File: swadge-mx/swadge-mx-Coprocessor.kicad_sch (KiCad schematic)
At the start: 6 parts, among them J4 Conn_02x05_Odd_Even, J5 Conn_02x05_Odd_Even, J6 Conn_02x05_Odd_Even, J7 Conn_02x05_Odd_Even, U7 CH32V003F4U6

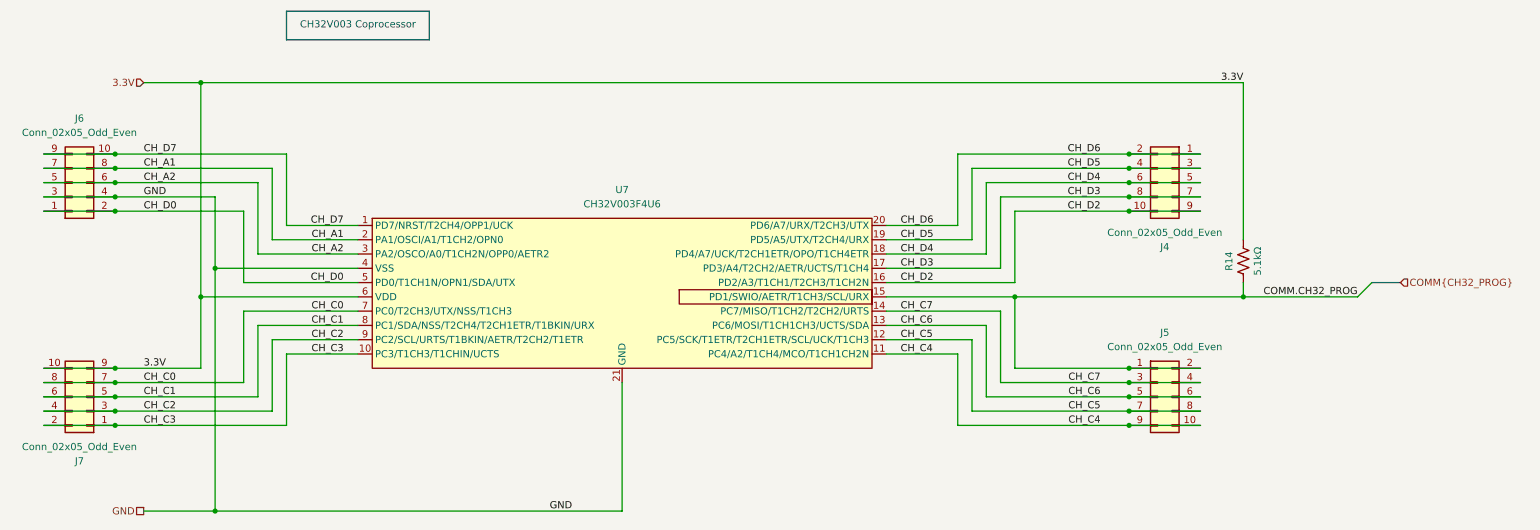
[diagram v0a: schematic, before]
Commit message: Further Subdivide Sheets
Moved all audio into one sheet, and sub-divided into DAC and amp sheets. Moved all power into one sheet and sub-divided into BMS and Buck.
Cleaned up front page a bit.
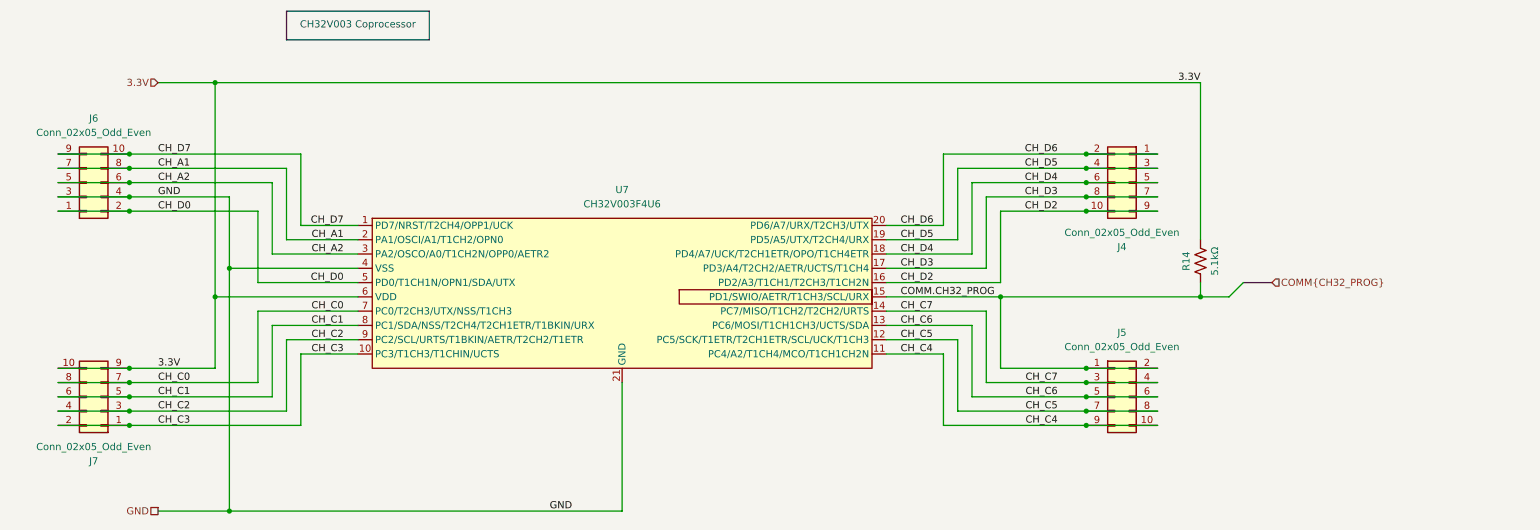
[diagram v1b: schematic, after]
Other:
- moved on the sheet: J4, J5, J6, J7, R14
